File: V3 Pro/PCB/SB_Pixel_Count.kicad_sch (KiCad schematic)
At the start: 19 parts, among them J2 String1, J3 OLED, SW1 Test, SW2 Test, U1 74AHCT1G125, U2 MOUDLE-SEEEDUINO-XIAO, U3 AMS1117-5.0, U4 INA219BxD, U5 TF-123-ARP9H17

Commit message: Add company name to title blocks; fix V3 Pro SW1/SW2 push-button DRC
Add (company "S&B Designs LLC") to V1/V2/V3 Pro's PCB and schematic
title blocks, matching V2 Lite, and add \${COMPANY} to each board's
silkscreen gr_text so it's printed on the physical board too.

Also includes KiCad-side board edits made while investigating the
SW1/SW2 "unconnected pad" DRC warnings on V3 Pro: added
lib/Scotts.pretty/SW_PUSH_6mm.kicad_mod, a copy of the standard
4-leg tactile switch footprint with unique pad numbers (1-4) instead
of the original's duplicated 1/1/2/2 numbering. The two redundant
mechanical-only legs (pads 3/4) are left with no net assigned, so
DRC's missing-connection check no longer applies to them. V3 Pro's
SW1/SW2 now use this footprint. Regenerated gerbers/BOM/fp-info-cache
reflect the resave.

Co-Authored-By: Claude Sonnet 5 <noreply@anthropic.com>
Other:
- company: (none) -> S&B Designs LLC
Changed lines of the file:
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@@
 		(date "2025-10-06")
 		(rev "v1")
+		(company "S&B Designs LLC")
 	)
 	(junction

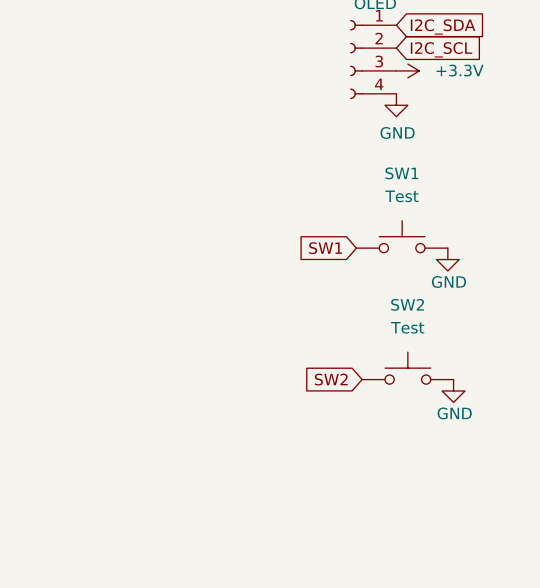
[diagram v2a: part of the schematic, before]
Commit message: Add 4-pin SW_PUSH_6mm schematic symbol, wire pin 4 to GND
New lib/Scotts.kicad_sym symbol for the 4-leg tactile switch, split
into two units: unit 1 (pins 1/2) is the actual switch contact, unit
2 (pins 3/4) represents the redundant mechanical legs. Registered in
V3 Pro's sym-lib-table.

SW1/SW2 now place both units: pin 4 (the redundant GND-side leg) is
wired to GND for a second physical ground connection, pin 3 (the
redundant switch-side leg) is flagged no-connect and left genuinely
netless on the PCB, matching the earlier footprint fix. Includes the
regenerated gerbers/BOM/fp-info-cache from the KiCad resave.

Co-Authored-By: Claude Sonnet 5 <noreply@anthropic.com>
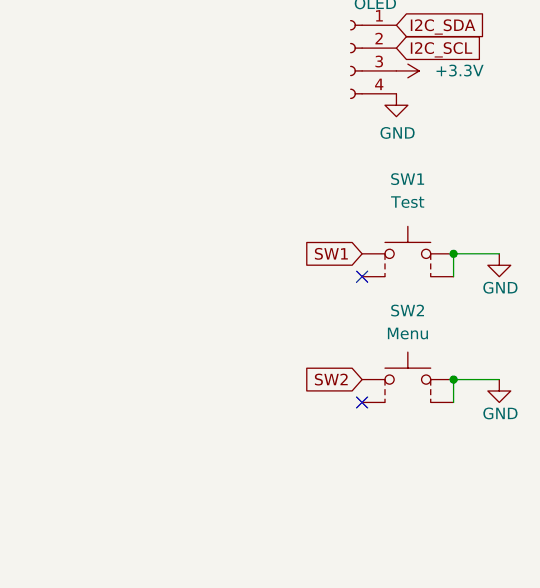
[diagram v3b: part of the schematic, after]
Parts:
- SW1: footprint Button_Switch_THT:SW_PUSH_6mm -> Scotts:SW_PUSH_6mm; symbol Switch:SW_Push -> Scotts:SW_PUSH_6mm
- SW2: value Test -> Menu; footprint Button_Switch_THT:SW_PUSH_6mm -> Scotts:SW_PUSH_6mm; symbol Switch:SW_Push -> Scotts:SW_PUSH_6mm
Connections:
- net GND: now also SW1.4, SW2.4
- no-connect marks 1 -> 3
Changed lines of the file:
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@@
+	)
+	(junction
+		(at 243.84 125.73)
+		(diameter 0)
+		(color 0 0 0 0)
 	)
 	(junction
@@
 	)
 	(junction
+		(at 243.84 139.7)
+		(diameter 0)
+		(color 0 0 0 0)
+	)
+	(junction
 		(at 137.16 163.83)
 		(diameter 0)
@@
 	)
 	(no_connect
+		(at 233.68 128.27)
+	)
+	(no_connect
+		(at 233.68 142.24)
+	)
+	(no_connect
 		(at 118.11 53.34)
 	)
@@
 	(wire
 		(pts
+			(xy 248.92 139.7) (xy 243.84 139.7)
+		)
+		(stroke
+			(width 0)
+			(type default)
+		)
+	)
+	(wire
+		(pts
+			(xy 243.84 139.7) (xy 243.84 142.24)
+		)
+		(stroke
+			(width 0)
+			(type default)
+		)
+	)
+	(wire
+		(pts
 			(xy 116.205 37.465) (xy 116.205 47.625)
 		)
@@
 	(wire
 		(pts
+			(xy 243.84 125.73) (xy 243.84 128.27)
+		)
+		(stroke
+			(width 0)
+			(type default)
+		)
+	)
+	(wire
+		(pts
 			(xy 137.16 161.29) (xy 137.16 163.83)
 		)
@@
 		(pts
 			(xy 95.25 60.325) (xy 97.155 60.325)
+		)
+		(stroke
+			(width 0)
+			(type default)
+		)
+	)
+	(wire
+		(pts
+			(xy 248.92 125.73) (xy 243.84 125.73)
 		)
 		(stroke
@@
 	(global_label "SW1"
 		(shape input)
-		(at 233.045 125.095 180)
+		(at 233.68 125.73 180)
 		(fields_autoplaced yes)
 		(effects
@@
 		)
 		(property "Intersheetrefs" "${INTERSHEET_REFS}"
-			(at 226.7614 125.1744 0)
+			(at 227.3964 125.8094 0)
 			(effects
 				(font
@@
 	(symbol
 		(lib_id "power:GND")
-		(at 243.84 139.7 0)
+		(at 248.92 139.7 0)
 		(unit 1)
 		(exclude_from_sim no)
@@
 		(dnp no)
 		(property "Reference" "#PWR018"
-			(at 243.84 146.05 0)
+			(at 248.92 146.05 0)
 			(effects
 				(font
@@
 		)
 		(property "Value" "GND"
-			(at 243.967 143.51 0)
+			(at 249.047 143.51 0)
 			(effects
 				(font
@@
 		)
 		(property "Footprint" ""
-			(at 243.84 139.7 0)
+			(at 248.92 139.7 0)
 			(effects
 				(font
@@
 		)
 		(property "Datasheet" ""
-			(at 243.84 139.7 0)
+			(at 248.92 139.7 0)
 			(effects
 				(font
@@
 		)
 		(property "Description" ""
-			(at 243.84 139.7 0)
+			(at 248.92 139.7 0)
 			(effects
 				(font
@@
 	)
 	(symbol
-		(lib_id "Switch:SW_Push")
+		(lib_id "Scotts:SW_PUSH_6mm")
 		(at 238.76 139.7 0)
 		(unit 1)
@@
 		(fields_autoplaced yes)
 		(property "Reference" "SW2"
-			(at 238.76 131.445 0)
-			(effects
-				(font
-					(size 1.27 1.27)
-				)
-			)
-		)
-		(property "Value" "Test"
-			(at 238.76 133.985 0)
-			(effects
-				(font
-					(size 1.27 1.27)
-				)
-			)
-		)
-		(property "Footprint" "Button_Switch_THT:SW_PUSH_6mm"
+			(at 238.76 132.08 0)
+			(effects
+				(font
+					(size 1.27 1.27)
+				)
+			)
+		)
+		(property "Value" "Menu"
+			(at 238.76 134.62 0)
+			(effects
+				(font
+					(size 1.27 1.27)
+				)
+			)
+		)
+		(property "Footprint" "Scotts:SW_PUSH_6mm"
 			(at 238.76 134.62 0)
 			(effects
@@
 			)
 		)
-		(property "Description" ""
+		(property "Description" "Push button switch, 4-leg THT 6mm tactile. Legs 3/4 are redundant mechanical duplicates of legs 1/2 (same nets internally) - left as no-connect since the footprint leaves those pads netless."
 			(at 238.76 139.7 0)
 			(effects
@@
 		)
 		(pin "2"
+		)
+		(pin "4"
+		)
+		(pin "3"
 		)
 		(instances
@@
 	(symbol
 		(lib_id "power:GND")
-		(at 243.205 125.095 0)
+		(at 248.92 125.73 0)
 		(unit 1)
 		(exclude_from_sim no)
@@
 		(dnp no)
 		(property "Reference" "#PWR011"
-			(at 243.205 131.445 0)
+			(at 248.92 132.08 0)
 			(effects
 				(font
@@
 		)
 		(property "Value" "GND"
-			(at 243.332 128.905 0)
+			(at 249.047 129.54 0)
 			(effects
 				(font
@@
 		)
 		(property "Footprint" ""
-			(at 243.205 125.095 0)
+			(at 248.92 125.73 0)
 			(effects
 				(font
@@
 		)
 		(property "Datasheet" ""
-			(at 243.205 125.095 0)
+			(at 248.92 125.73 0)
 			(effects
 				(font
@@
 		)
 		(property "Description" ""
-			(at 243.205 125.095 0)
+			(at 248.92 125.73 0)
 			(effects
 				(font
@@
 	)
 	(symbol
-		(lib_id "Switch:SW_Push")
-		(at 238.125 125.095 0)
+		(lib_id "Scotts:SW_PUSH_6mm")
+		(at 238.76 125.73 0)
 		(unit 1)
 		(exclude_from_sim no)
@@
 		(fields_autoplaced yes)
 		(property "Reference" "SW1"
-			(at 238.125 116.84 0)
+			(at 238.76 117.475 0)
 			(effects
 				(font
@@
 		)
 		(property "Value" "Test"
-			(at 238.125 119.38 0)
-			(effects
-				(font
-					(size 1.27 1.27)
-				)
-			)
-		)
-		(property "Footprint" "Button_Switch_THT:SW_PUSH_6mm"
-			(at 238.125 120.015 0)
+			(at 238.76 120.015 0)
+			(effects
+				(font
+					(size 1.27 1.27)
+				)
+			)
+		)
+		(property "Footprint" "Scotts:SW_PUSH_6mm"
+			(at 238.76 120.65 0)
 			(effects
 				(font
@@
 		)
 		(property "Datasheet" "~"
-			(at 238.125 120.015 0)
-			(effects
-				(font
-					(size 1.27 1.27)
-				)
-				(hide yes)
-			)
-		)
-		(property "Description" ""
-			(at 238.125 125.095 0)
+			(at 238.76 120.65 0)
+			(effects
+				(font
+					(size 1.27 1.27)
+				)
+				(hide yes)
+			)
+		)
+		(property "Description" "Push button switch, 4-leg THT 6mm tactile. Legs 3/4 are redundant mechanical duplicates of legs 1/2 (same nets internally) - left as no-connect since the footprint leaves those pads netless."
+			(at 238.76 125.73 0)
 			(effects
 				(font
@@
 		)
 		(property "LCSC" "C2834918"
-			(at 238.125 125.095 0)
+			(at 238.76 125.73 0)
 			(effects
 				(font
@@
 		)
 		(property "Digi-Key_PN" "CKN10880CT-ND"
-			(at 238.125 125.095 0)
+			(at 238.76 125.73 0)
 			(effects
 				(font
@@
 		)
 		(property "MPN" "PTS645SL43SMTR92 LFS"
-			(at 238.125 125.095 0)
+			(at 238.76 125.73 0)
 			(effects
 				(font
@@
 		(pin "2"
 		)
+		(pin "3"
+		)
+		(pin "4"
+		)
 		(instances
